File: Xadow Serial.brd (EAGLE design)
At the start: 28.1 x 20.3 mm, 28 parts, among them J1 CONNECTOR-HEADER-8P-3461050P1, J2 12p 0.5mm bottom contact, J3 12p 0.5mm bottom contact, J4 12p 0.5mm bottom contact, U1 SC16IS750, U2 BSS138PS, X1 CTS_32X25_SMD

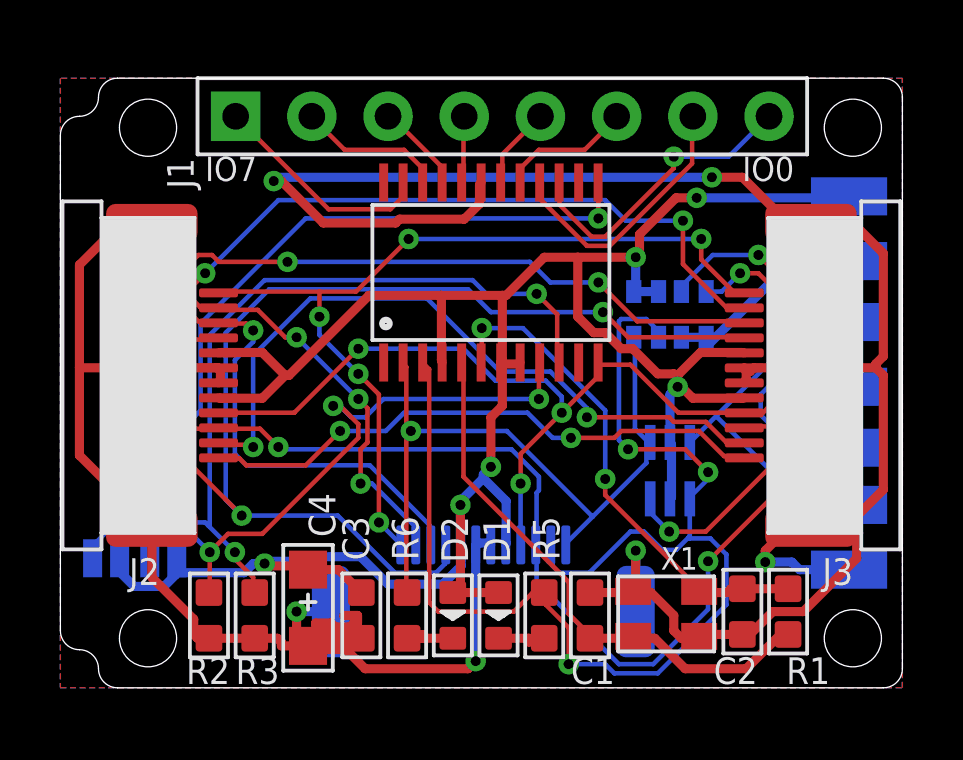
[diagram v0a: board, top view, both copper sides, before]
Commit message: Better crystal location
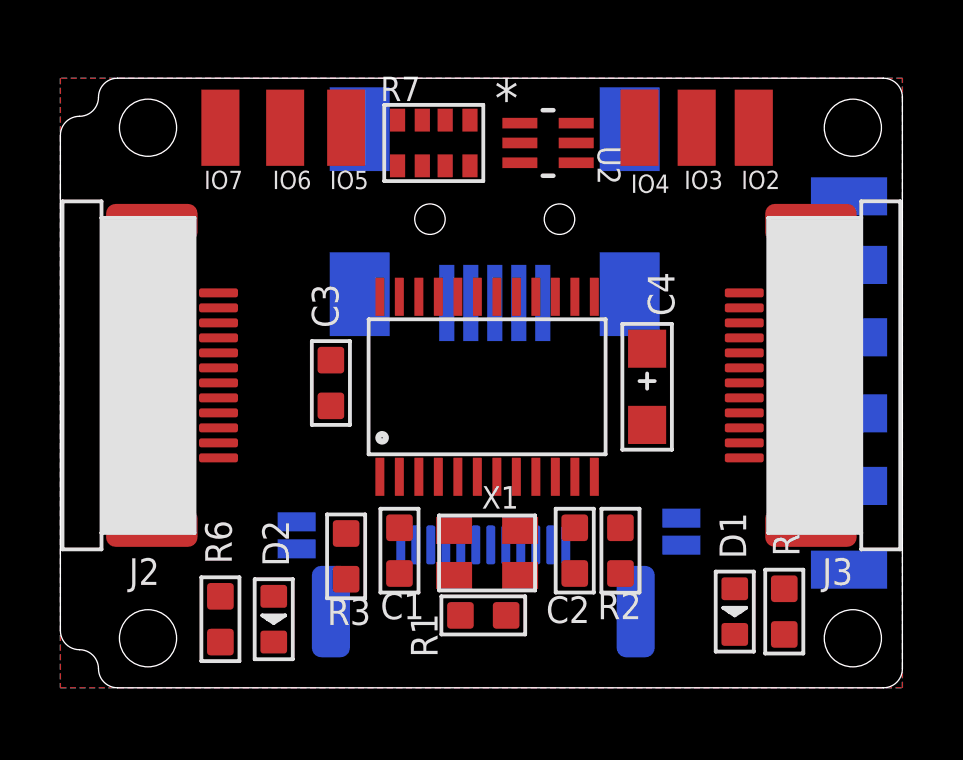
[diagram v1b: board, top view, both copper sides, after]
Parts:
- removed 5V, RX_5, TX_5: WIREPADSMD1,27-254, wirepad:SMD1,27-2,54
- removed J1: CONNECTOR-HEADER-8P-3461050P1, OPL:1X8P-2.54-2.54-11.6-3.0-BALCK-MALE
- added IO0, IO1, IO2, IO3, IO4, IO5, IO6, IO7: WIREPADSMD1,27-254, wirepad:SMD1,27-2,54
- added J5: MINI-USB-5P-3400020P1, Connector:MINI-B-SMD
- moved A0 17.3 mm to (20.8, 5.33), turned to 270 degrees
- moved R2 13.9 mm to (18.8, 4.70)
- moved C4 13.5 mm to (19.7, 10.2)
- moved U2 11.7 mm to (16.4, 18.3), flipped to the top, turned to 0 degrees
- moved R1 10.2 mm to (14.2, 2.54), turned to 0 degrees
- moved R7 9.73 mm to (12.6, 18.3), flipped to the top
- moved R5 8.00 mm to (24.3, 2.67)
- moved D1 7.88 mm to (22.6, 2.67)
- moved C3 7.81 mm to (9.14, 10.3)
- moved C1 6.71 mm to (11.4, 4.70)
- moved A1 6.40 mm to (8.00, 5.21), turned to 90 degrees
- moved X1 6.31 mm to (14.4, 4.57)
- moved R6 6.22 mm to (5.46, 2.41)
- moved D2 5.97 mm to (7.24, 2.41)
- moved C2 5.95 mm to (17.3, 4.70)
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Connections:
- net 5V: now also J5.1; no longer 5V.1
- net GND: now also J5.5, J5.P$1, J5.P$2, J5.P$3, J5.P$4
- net IO0: now also IO0.1, J5.2; no longer J1.8
- net IO1: now also IO1.1, J5.4; no longer J1.7
- net IO2: now also IO2.1; no longer J1.6
- net IO3: now also IO3.1; no longer J1.5
- net IO4: now also IO4.1; no longer J1.4
- net IO5: now also IO5.1; no longer J1.3
- net IO6: now also IO6.1; no longer J1.2
- net IO7: now also IO7.1; no longer J1.1
- net RX_5: no longer RX_5.1
- net TX_5: now also J5.3; no longer TX_5.1
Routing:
- net GND: track 115.5 -> 0.00 mm, vias 6 -> 0
- net 3V3: track 81.3 -> 0.00 mm, vias 6 -> 0
- net PD1/SDA/D2: track 56.9 -> 0.00 mm, vias 5 -> 0
- net RX: track 42.5 -> 0.00 mm, vias 3 -> 0
- net PF0/A5: track 41.5 -> 0.00 mm, vias 4 -> 0
- net PB3/D14/MISO: track 36.3 -> 0.00 mm, vias 3 -> 0
- net PB2/D16/MOSI: track 35.4 -> 0.00 mm, vias 5 -> 0
- net PD0/SCL/D3: track 30.1 -> 0.00 mm, vias 4 -> 0
- net PB1/D15/SCK: track 29.0 -> 0.00 mm, vias 5 -> 0
- net N$3: track 28.4 -> 0.00 mm, vias 2 -> 0
- net PD2/RXI/D0: track 23.6 -> 0.00 mm, vias 2 -> 0
- net TX: track 23.5 -> 0.00 mm, vias 1 -> 0
- net N$4: track 20.8 -> 0.00 mm, vias 3 -> 0
- net TX_5: track 19.6 -> 0.00 mm, vias 4 -> 0
- net PD3/TXO/D1: track 19.2 -> 0.00 mm, vias 2 -> 0
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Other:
- board text removed: "IO0"
- board text removed: "IO1"
- board text removed: "IO2"
- board text removed: "IO3"
- board text removed: "IO4"
- board text removed: "IO5"
- board text removed: "IO6"
- board text removed: "IO7"

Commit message: Some more component position fiddling
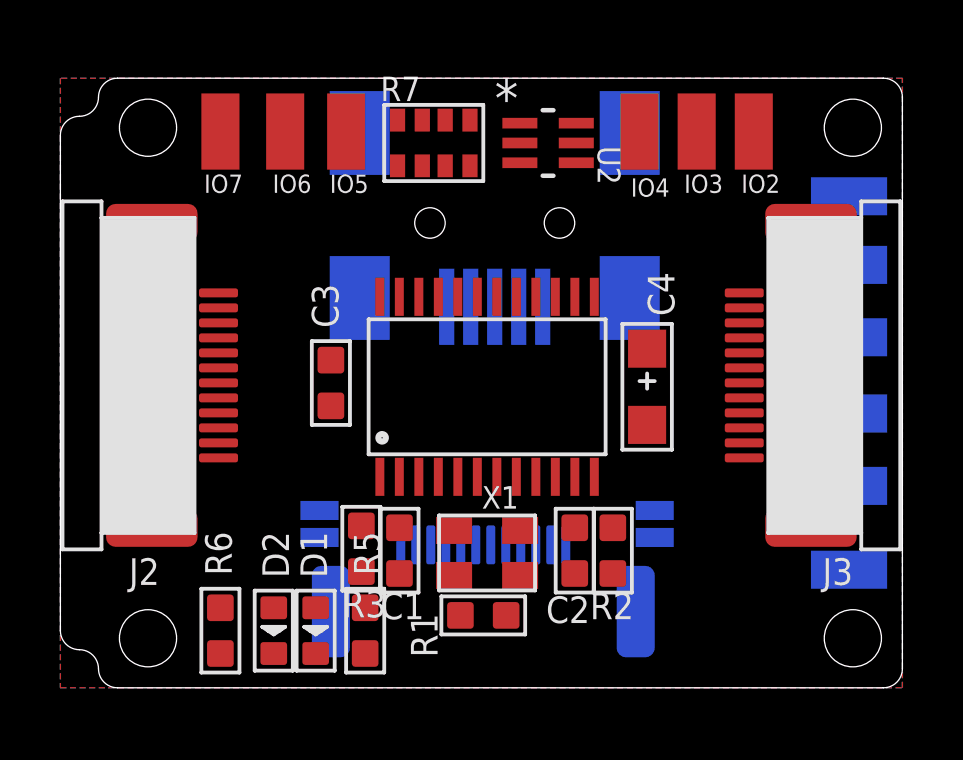
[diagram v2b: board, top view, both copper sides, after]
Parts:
- moved D1 14.0 mm to (8.64, 2.03)
- moved R5 14.0 mm to (10.3, 2.03)
- moved A0 0.92 mm to (19.9, 5.59), turned to 90 degrees
- moved A1 0.85 mm to (8.76, 5.59)
- moved R3 0.57 mm to (10.2, 4.76)
- moved D2 0.38 mm to (7.24, 2.03)
- moved R6 0.38 mm to (5.46, 2.03)
- moved R2 0.25 mm to (18.5, 4.70)
- moved IO2 0.13 mm to (23.2, 18.7)
- moved IO3 0.13 mm to (21.3, 18.7)
- moved IO4 0.13 mm to (19.4, 18.7)
- moved IO5 0.13 mm to (9.65, 18.7)
- moved IO6 0.13 mm to (7.62, 18.7)
- moved IO7 0.13 mm to (5.46, 18.7)
- moved J5 0.13 mm to (14.6, 17.0)

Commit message: Routed to OSHPark DRU and sent for fab
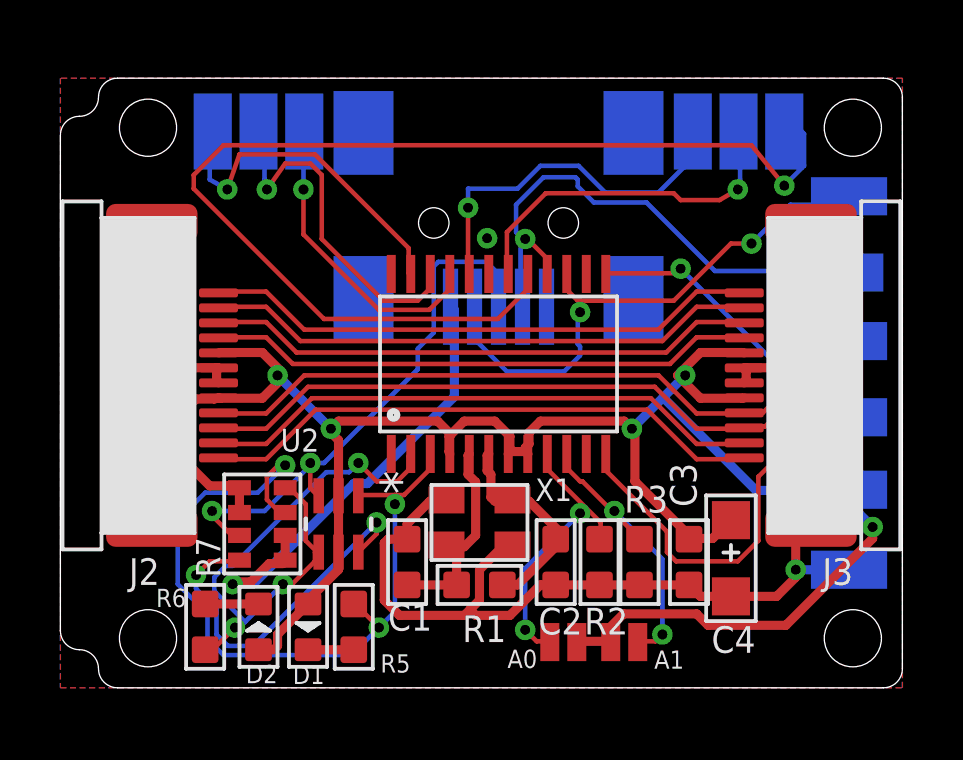
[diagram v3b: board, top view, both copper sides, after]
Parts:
- removed J4: 12p 0.5mm bottom contact, template:12P-0.5
- C1, C2: value 18pF -> 26pF
- moved U2 14.5 mm to (9.40, 5.59), turned to 270 degrees
- moved R7 13.9 mm to (6.86, 5.59), turned to 90 degrees
- moved C3 13.3 mm to (21.1, 4.32)
- moved A1 10.9 mm to (18.9, 1.65), flipped to the top, turned to 0 degrees
- moved 3V3 9.78 mm to (26.4, 6.73)
- moved IO0 9.65 mm to (26.4, 16.5)
- moved R3 9.28 mm to (19.4, 4.32)
- moved C4 6.36 mm to (22.5, 4.45)
- moved A0 4.98 mm to (16.9, 1.65), flipped to the top, turned to 180 degrees
- moved IO1 4.70 mm to (26.3, 14.0)
- moved SDA 2.67 mm to (26.4, 9.14)
- moved SCL 2.54 mm to (26.4, 11.7)
- moved IO4 1.78 mm to (21.2, 18.7), flipped to the bottom, turned to 180 degrees
- moved IO3 1.40 mm to (22.7, 18.7), flipped to the bottom, turned to 180 degrees
- moved IO5 1.40 mm to (8.26, 18.7), flipped to the bottom, turned to 180 degrees
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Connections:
- net 3V3: no longer J4.5, J4.8
- net GND: no longer J4.6, J4.7, J4.P1, J4.P2
- net PB1/D15/SCK: no longer J4.12
- net PB2/D16/MOSI: no longer J4.11
- net PB3/D14/MISO: no longer J4.10
- net PD0/SCL/D3: no longer J4.4
- net PD1/SDA/D2: no longer J4.3
- net PF0/A5: no longer J4.9
- net RX: no longer J4.2
- net TX: no longer J4.1
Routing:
- net 3V3: track 0.00 -> 71.4 mm, vias 0 -> 5
- net GND: track 0.00 -> 57.8 mm, vias 0 -> 2
- net IO2: track 0.00 -> 37.8 mm, vias 0 -> 1
- net PD0/SCL/D3: track 0.00 -> 36.2 mm, vias 0 -> 1
- net PD1/SDA/D2: track 0.00 -> 31.4 mm, vias 0 -> 2
- net RX: track 0.00 -> 26.5 mm, vias 0 -> 3
- net TX: track 0.00 -> 19.0 mm, vias 0 -> 3
- net PD3/TXO/D1: track 0.00 -> 18.9 mm
- net PD2/RXI/D0: track 0.00 -> 18.8 mm
- net IO0: track 0.00 -> 18.7 mm, vias 0 -> 2
- net PB1/D15/SCK: track 0.00 -> 18.6 mm
- net TX_5: track 0.00 -> 18.6 mm, vias 0 -> 2
- net PB2/D16/MOSI: track 0.00 -> 18.5 mm
- net PB3/D14/MISO: track 0.00 -> 18.4 mm
- net PF0/A5: track 0.00 -> 18.3 mm
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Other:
- board text added: "v2.0 15/10/2014"
- board text removed: "v1.0 15/10/2014"

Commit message: Converted to use SPI
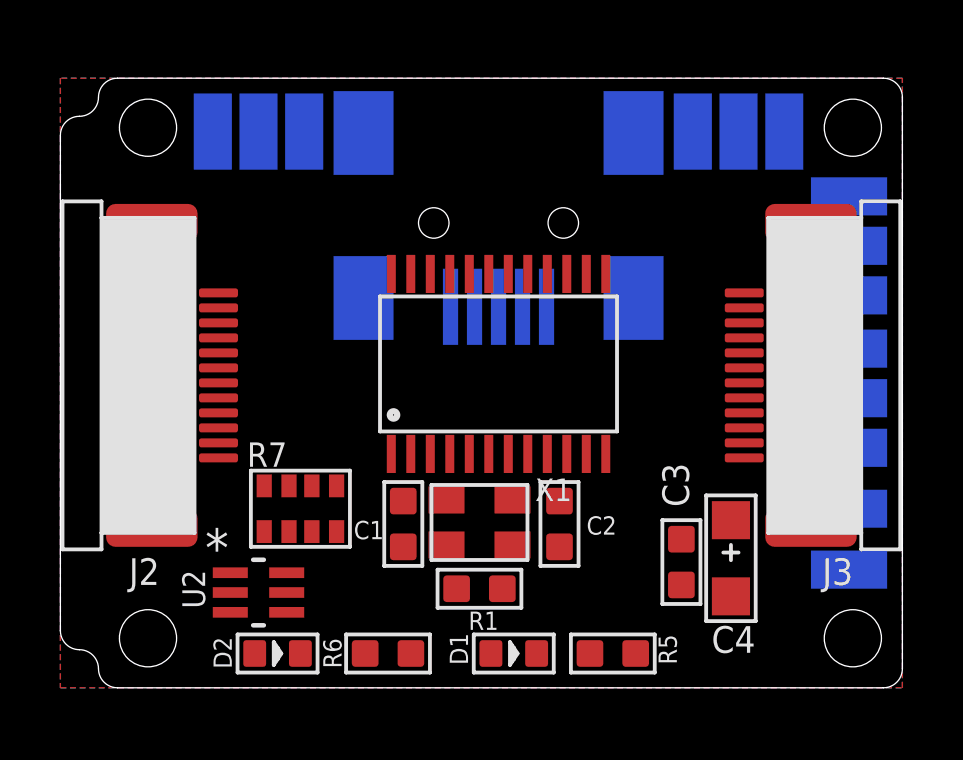
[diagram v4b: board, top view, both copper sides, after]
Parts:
- removed A0, A1: JUMPER-PAD-2-NO, SparkFun-Passives:PAD-JUMPER-2-NO_NO_SILK
- removed R2, R3: 10K, OPL:R0603
- removed SCL, SDA: WIREPADSMD1,27-254, wirepad:SMD1,27-2,54
- added CLK, CS, SI, SO: WIREPADSMD1,27-254, wirepad:SMD1,27-2,54
- moved R5 8.68 mm to (18.5, 1.27), turned to 180 degrees
- moved D1 6.92 mm to (15.2, 1.27), turned to 0 degrees
- moved R6 6.16 mm to (11.0, 1.27), turned to 180 degrees
- moved U2 3.51 mm to (6.73, 3.30), turned to 0 degrees
- moved R7 1.37 mm to (8.13, 6.10), turned to 0 degrees
- moved C1 1.28 mm to (11.6, 5.59)
- moved C2 1.28 mm to (16.8, 5.59)
- moved D2 1.09 mm to (7.37, 1.27), turned to 0 degrees
- moved IO1 0.90 mm to (26.4, 14.9)
- moved 3V3 0.63 mm to (26.4, 6.10)
- moved C3 0.25 mm to (20.8, 4.32)
- moved R1 0.13 mm to (14.1, 3.43)
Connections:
- removed net N$3: A1.2, R3.1, U1.P$10
- removed net N$4: A0.2, R2.1, U1.P$9
- net 3V3: no longer A0.1, A1.1, U1.P$8
- net GND: now also U1.P$13, U1.P$8; no longer R2.2, R3.2
- net PB1/D15/SCK: now also CLK.1, U1.P$12
- net PB2/D16/MOSI: now also SI.1, U1.P$10
- net PB3/D14/MISO: now also SO.1, U1.P$11
- net PD0/SCL/D3: no longer SCL.1, U1.P$12
- net PD1/SDA/D2: no longer SDA.1, U1.P$13
- net PF0/A5: now also CS.1, U1.P$9
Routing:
- net 3V3: track 71.4 -> 0.00 mm, vias 5 -> 0
- net GND: track 57.8 -> 0.00 mm, vias 2 -> 0
- net IO2: track 37.8 -> 0.00 mm, vias 1 -> 0
- net PD0/SCL/D3: track 36.2 -> 0.00 mm, vias 1 -> 0
- net PD1/SDA/D2: track 31.4 -> 0.00 mm, vias 2 -> 0
- net RX: track 26.5 -> 0.00 mm, vias 3 -> 0
- net TX: track 19.0 -> 0.00 mm, vias 3 -> 0
- net PD3/TXO/D1: track 18.9 -> 0.00 mm
- net PD2/RXI/D0: track 18.8 -> 0.00 mm
- net IO0: track 18.7 -> 0.00 mm, vias 2 -> 0
- net PB1/D15/SCK: track 18.6 -> 0.00 mm
- net TX_5: track 18.6 -> 0.00 mm, vias 2 -> 0
- net PB2/D16/MOSI: track 18.5 -> 0.00 mm
- net PB3/D14/MISO: track 18.4 -> 0.00 mm
- net PF0/A5: track 18.3 -> 0.00 mm
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
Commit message: Finished routing in SPI mode
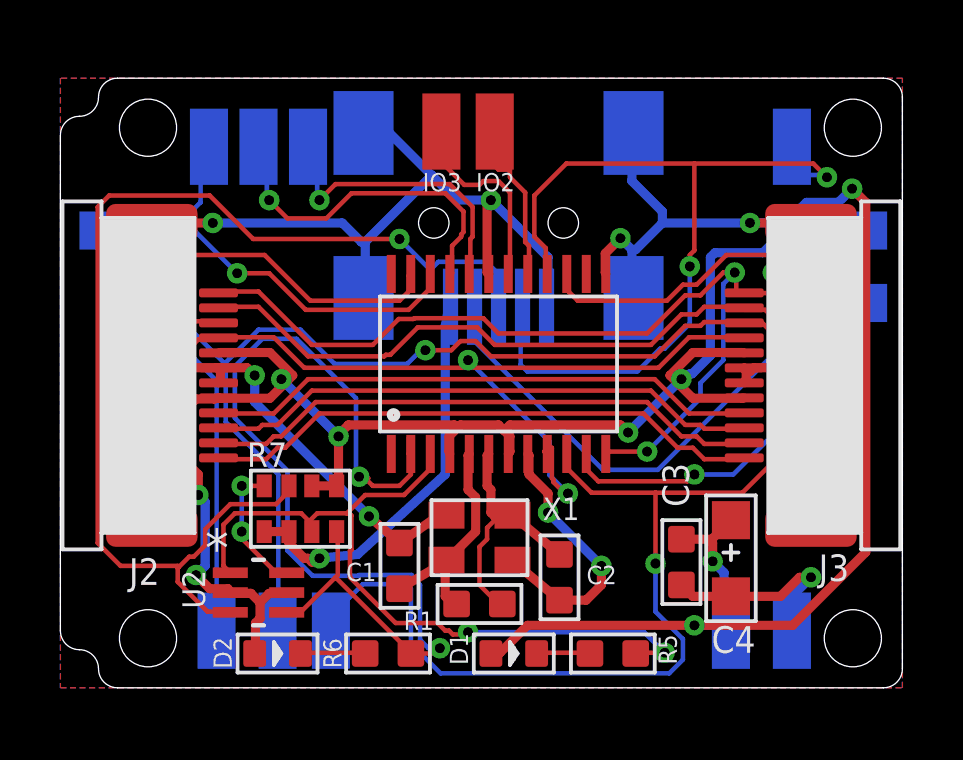
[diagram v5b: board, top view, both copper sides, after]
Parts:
- moved CS 21.9 mm to (5.33, 2.03), turned to 180 degrees
- moved SO 20.6 mm to (7.37, 2.03), turned to 180 degrees
- moved SI 19.7 mm to (9.14, 2.03), turned to 180 degrees
- moved IO4 12.8 mm to (8.38, 18.2)
- moved IO3 9.91 mm to (12.8, 18.7), flipped to the top
- moved IO2 9.65 mm to (14.6, 18.7), flipped to the top
- moved 3V3 5.66 mm to (22.5, 2.03), turned to 0 degrees
- moved IO7 4.58 mm to (2.03, 15.4), turned to 90 degrees
- moved IO1 3.81 mm to (24.5, 18.2), turned to 0 degrees
- moved GND 2.79 mm to (24.5, 2.03), turned to 0 degrees
- moved C2 1.78 mm to (16.8, 3.81)
- moved IO6 1.73 mm to (5.08, 18.2)
- moved IO5 1.61 mm to (6.73, 18.2)
- moved C1 1.40 mm to (11.4, 4.19)
- moved IO0 1.14 mm to (26.4, 15.4)
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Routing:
- net GND: track 0.00 -> 94.8 mm, vias 0 -> 9
- net 3V3: track 0.00 -> 86.9 mm, vias 0 -> 9
- net PB2/D16/MOSI: track 0.00 -> 55.7 mm, vias 0 -> 3
- net PB3/D14/MISO: track 0.00 -> 45.7 mm, vias 0 -> 4
- net TX_5: track 0.00 -> 38.1 mm, vias 0 -> 1
- net PF0/A5: track 0.00 -> 38.0 mm, vias 0 -> 3
- net TX: track 0.00 -> 34.0 mm, vias 0 -> 2
- net PB1/D15/SCK: track 0.00 -> 32.6 mm, vias 0 -> 3
- net IO0: track 0.00 -> 29.4 mm, vias 0 -> 1
- net IO1: track 0.00 -> 28.8 mm, vias 0 -> 2
- net RX: track 0.00 -> 25.4 mm, vias 0 -> 2
- net PD3/TXO/D1: track 0.00 -> 18.8 mm
- net PD2/RXI/D0: track 0.00 -> 18.7 mm
- net PD1/SDA/D2: track 0.00 -> 18.6 mm
- net PD0/SCL/D3: track 0.00 -> 18.5 mm
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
